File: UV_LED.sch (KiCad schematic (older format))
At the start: 64 parts, among them IC1 ATMEGA328P-A, P1 12Vin, P2 USB_A, P3 CONN_01X16, P4 VACUUM, P5 LED_TOP, P6 LED_BOTTOM, Q1 MOSFET_N, Q2 MOSFET_N, Q3 MOSFET_N, Q4 MMBT3906, SW1 SPST, U1 FT232RL, U2 ACT4060A, U3 MPXV6115V, U4 PCF8574, X1 16mHz

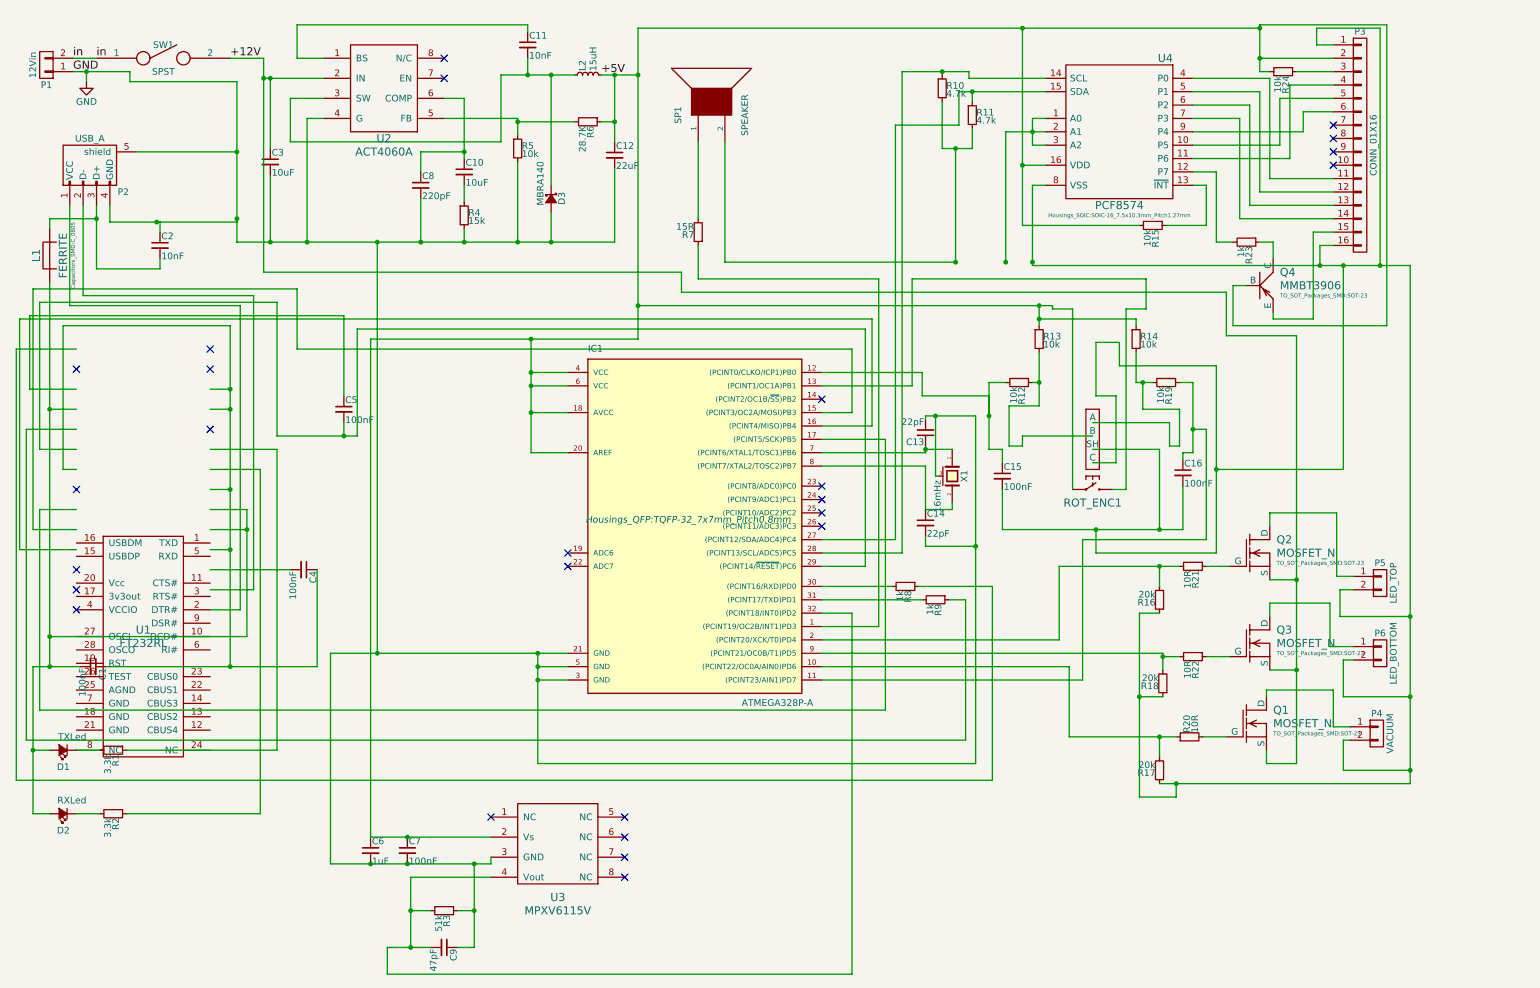
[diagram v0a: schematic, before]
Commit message: schematic changes, new pcb
simplified the schematic, added reset button, remade pcb for easier
home processing
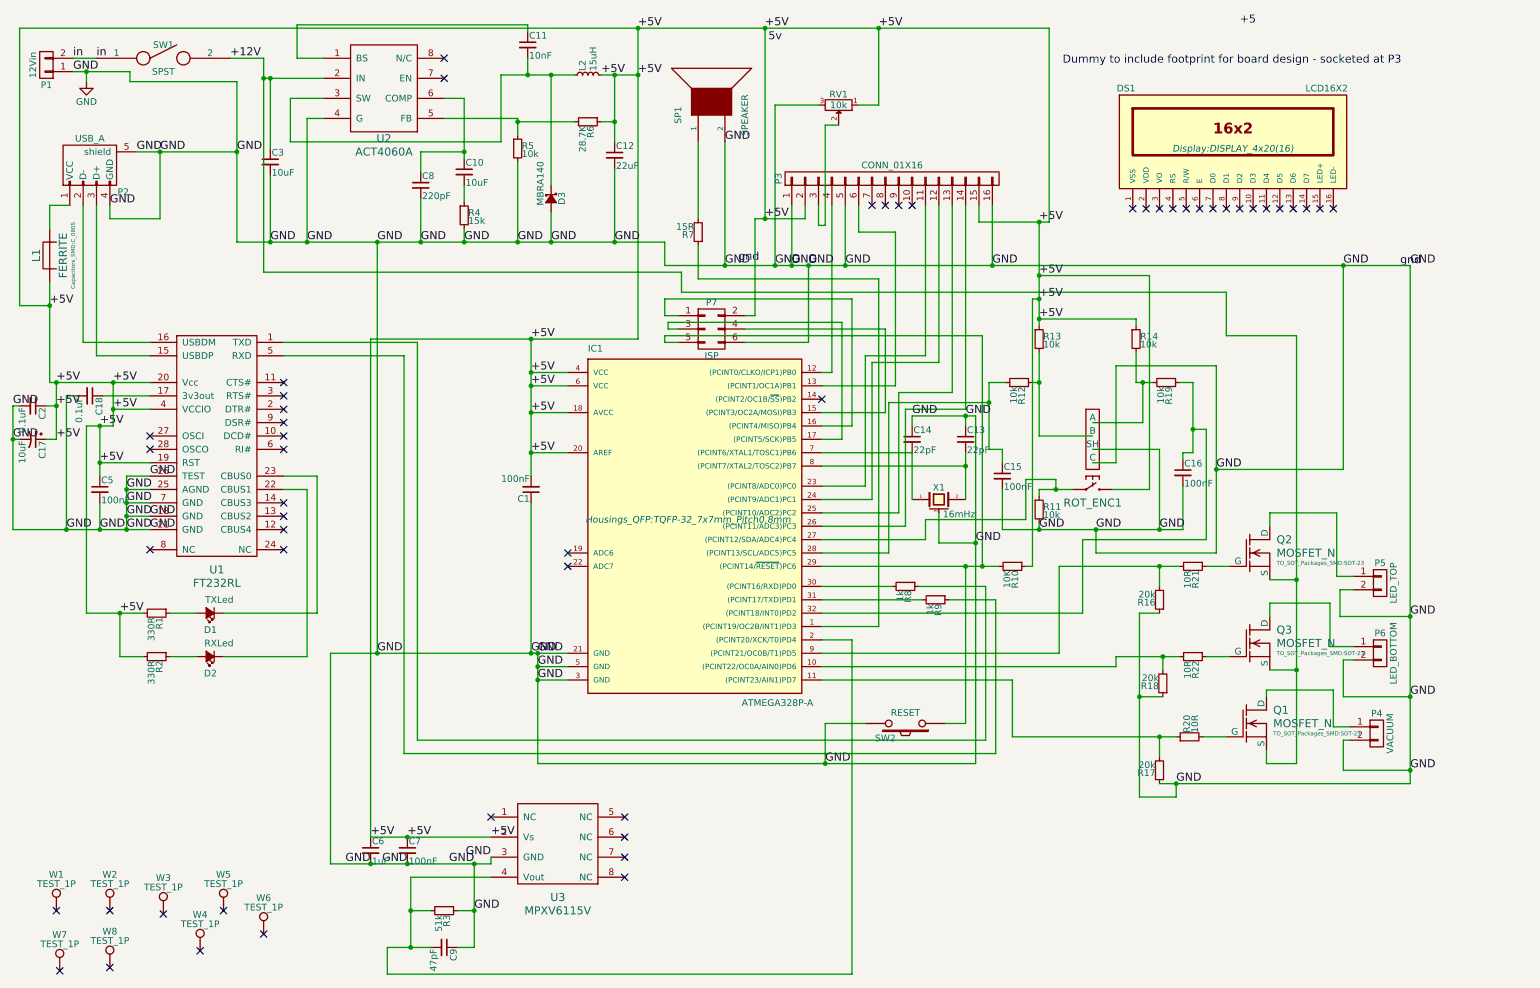
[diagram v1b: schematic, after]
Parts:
- removed C4: 100nF, Capacitors_SMD:C_0805, symbol C_Small
- removed Q4: MMBT3906, TO_SOT_Packages_SMD:SOT-23, symbol PNP
- removed R15, R24: 10k, Resistors_SMD:R_0805, symbol R_Small
- removed R23: 1k, Resistors_SMD:R_0805, symbol R_Small
- removed U4: PCF8574, Housings_SOIC:SOIC-16_7.5x10.3mm_Pitch1.27mm, symbol PCF8574
- added C17: 10uF, Capacitors_Tantalum_SMD:TantalC_SizeB_EIA-3528_Reflow, symbol CP1_Small
- added C18: 0.1uF, Capacitors_SMD:C_0805, symbol C_Small
- added DS1: LCD16X2, Display:DISPLAY_4x20(16), symbol LCD16X2
- added P7: ISP, Pin_Headers:Pin_Header_Straight_2x03, symbol CONN_02X03
- added RV1: 10k, TC33X-2-103E:35WR, symbol POT
- added SW2: RESET, Buttons_Switches_ThroughHole:Push_E-Switch_KS01Q01, symbol SW_PUSH
- added W1, W2, W7, W8: TEST_1P, Mounting_Holes:MountingHole_2-5mm, symbol TEST_1P
- added W3, W4, W5, W6: TEST_1P, Mounting_Holes:MountingHole_4mm, symbol TEST_1P
- C2: value 10nF -> 0.1uF
- P3: footprint Pin_Headers:Pin_Header_Angled_1x16 -> Display:Pin_Header_Angled_1x16_backward
- R1, R2: value 3.3k -> 330R
- R10: value 4.7k -> 10K
- R11: value 4.7k -> 10k
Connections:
- wire segments 373 -> 321
- no-connect marks 26 -> 51
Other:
- note added: "+5"
- note added: "5v"
- note added: "Dummy to include footprint for board design - socketed at P3"
- note added: "gnd"
- moved on the sheet: C1, C13, C14, C5, D1, D2, P3, R1, R2, X1

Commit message: added renders, rerouted PCB
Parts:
- U1: symbol FT232RL -> FT232RL-RESCUE-UV_LED
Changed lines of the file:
@@
 EESchema Schematic File Version 2
+LIBS:UV_LED-rescue
+LIBS:74xgxx
 LIBS:74xx
-LIBS:switcher
-LIBS:adc-dac
-LIBS:analog-switches
-LIBS:atmel
-LIBS:bjt
-LIBS:can
-LIBS:capacitive
-LIBS:cmos4000
-LIBS:conn
-LIBS:device
-LIBS:digital-audio
-LIBS:digpot
-LIBS:diode
-LIBS:display
-LIBS:fet
-LIBS:hc11
-LIBS:i2c
-LIBS:inductive
-LIBS:intel
-LIBS:interface
-LIBS:linear
-LIBS:memory
-LIBS:microchip
-LIBS:opto
-LIBS:periph
-LIBS:power
-LIBS:protection
-LIBS:regul
-LIBS:renesas
-LIBS:resist
-LIBS:supervisor
-LIBS:video
-LIBS:figaro
-LIBS:radio
-LIBS:automation
-LIBS:graphic
-LIBS:xilinx
-LIBS:UV_LED
-LIBS:switch-enc
 LIBS:ab2_7segment
 LIBS:ab2_audio
@@
 LIBS:ab2_usb
 LIBS:ab2_xtal
+LIBS:ac-dc
+LIBS:actel
+LIBS:adc-dac
+LIBS:Altera
+LIBS:analog_devices
+LIBS:analog_switches
+LIBS:analog-switches
+LIBS:arduino_shieldsNCL
+LIBS:atmel
+LIBS:audio
+LIBS:automation
+LIBS:bjt
+LIBS:brooktre
+LIBS:can
+LIBS:capacitive
+LIBS:cmos_ieee
+LIBS:cmos4000
+LIBS:conn
+LIBS:contrib
+LIBS:custom
+LIBS:cypress
+LIBS:dc-dc
+LIBS:device
+LIBS:digital-audio
+LIBS:digpot
+LIBS:diode
+LIBS:DIP28
+LIBS:DIP30
+LIBS:display
+LIBS:ds3231n
+LIBS:dsp
+LIBS:elec-unifil
+LIBS:ESD_Protection
+LIBS:FE
+LIBS:fet_driver
+LIBS:fet
+LIBS:figaro
+LIBS:fluid
+LIBS:ftdi
+LIBS:gennum
+LIBS:graphic
+LIBS:HALL-TLE4935G
+LIBS:HALL-TLE4935L
+LIBS:hc11
+LIBS:i2c
+LIBS:inductive
+LIBS:intel
+LIBS:interface
+LIBS:ir
+LIBS:jmp
+LIBS:Lattice
+LIBS:linear
+LIBS:lm1117
+LIBS:logo
+LIBS:LPC11xx_HVQFN33
+LIBS:lpcxpresso_1769_header
+LIBS:m-bed
+LIBS:maxim
+LIBS:mcp230xx
+LIBS:mech-switch
+LIBS:memory
+LIBS:microchip_dspic33dsc
+LIBS:microchip_pic10mcu
+LIBS:microchip_pic12mcu
+LIBS:microchip_pic16mcu
+LIBS:microchip_pic18mcu
+LIBS:microchip_pic32mcu
+LIBS:microchip
+LIBS:microcontrollers
+LIBS:microsd_attend_molex
+LIBS:microsd-molex
+LIBS:motor_drivers
+LIBS:motorola
+LIBS:msp430
+LIBS:nordicsemi
+LIBS:nxp_armmcu
+LIBS:onsemi
+LIBS:opendous
+LIBS:opto
+LIBS:optoendstops
+LIBS:Oscillators
+LIBS:pca9685
+LIBS:periph
+LIBS:philips
+LIBS:pololu_a4988x
+LIBS:Power_Management
+LIBS:power-switches
+LIBS:power
+LIBS:powerint
+LIBS:protection
+LIBS:pspice
+LIBS:radio
+LIBS:references
+LIBS:regul
+LIBS:relays
+LIBS:renesas
+LIBS:resist
+LIBS:rfcom
+LIBS:RMC_connectors
+LIBS:RMC
+LIBS:sensors
+LIBS:silabs
+LIBS:siliconi
+LIBS:stepper_drivers
+LIBS:stm8
+LIBS:stm32
+LIBS:STM32F100_48
+LIBS:STM32F429 LQFP144
+LIBS:supertex
+LIBS:supervisor
+LIBS:switch-enc
+LIBS:switcher
+LIBS:switches
+LIBS:TC33X-2-103E
+LIBS:texas
+LIBS:transf
+LIBS:transistors
+LIBS:ttl_ieee
+LIBS:valves
+LIBS:video
+LIBS:Worldsemi
+LIBS:Xicor
+LIBS:xilinx
+LIBS:Zilog
+LIBS:Symbols_DCDC-ACDC-Converter_RevC_20Jul2012
+LIBS:Symbols_EN60617_13Mar2013
+LIBS:Symbols_EN60617-10_HF-Radio_DRAFT_12Sep2013
+LIBS:Symbols_ICs-Diskrete_RevD10
+LIBS:Symbols_ICs-Opto_RevB_16Sep2013
+LIBS:Symbols_Microcontroller_Philips-NXP_RevA_06Oct2013
+LIBS:Symbols_Socket-DIN41612_RevA
+LIBS:Symbols_Transformer-Diskrete_RevA
+LIBS:SymbolsSimilarEN60617+oldDIN617-RevE8
 LIBS:UV_LED-cache
 EELAYER 25 0
@@
 +5V
 $Comp
-L GND #PWR01
+L GND-RESCUE-UV_LED #PWR01
 U 1 1 56E95E4B
 P 1075 950
@@
 $EndComp
 $Comp
-L FT232RL U1
+L FT232RL-RESCUE-UV_LED U1
 U 1 1 56F8DF31
 P 2050 3700
